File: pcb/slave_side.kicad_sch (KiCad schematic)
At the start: 71 parts, among them IC2 PCA9956BTWY, J4 4P4C_Shielded, SW20 SW_Push_45deg, SW21 SW_Push_45deg, SW22 SW_Push_45deg, SW23 SW_Push_45deg, SW24 SW_Push_45deg, SW25 SW_Push_45deg, SW26 SW_Push_45deg, SW27 SW_Push_45deg, SW28 SW_Push_45deg, SW29 SW_Push_45deg, SW30 SW_Push_45deg, SW31 SW_Push_45deg, SW32 SW_Push_45deg, SW33 SW_Push_45deg, SW34 SW_Push_45deg, SW35 SW_Push_45deg, SW36 SW_Push_45deg, SW37 SW_Push_45deg, U5 MCP23017T-E/ML, U6 NCP1117LPST33T3G, U7 OPT3001DNPR

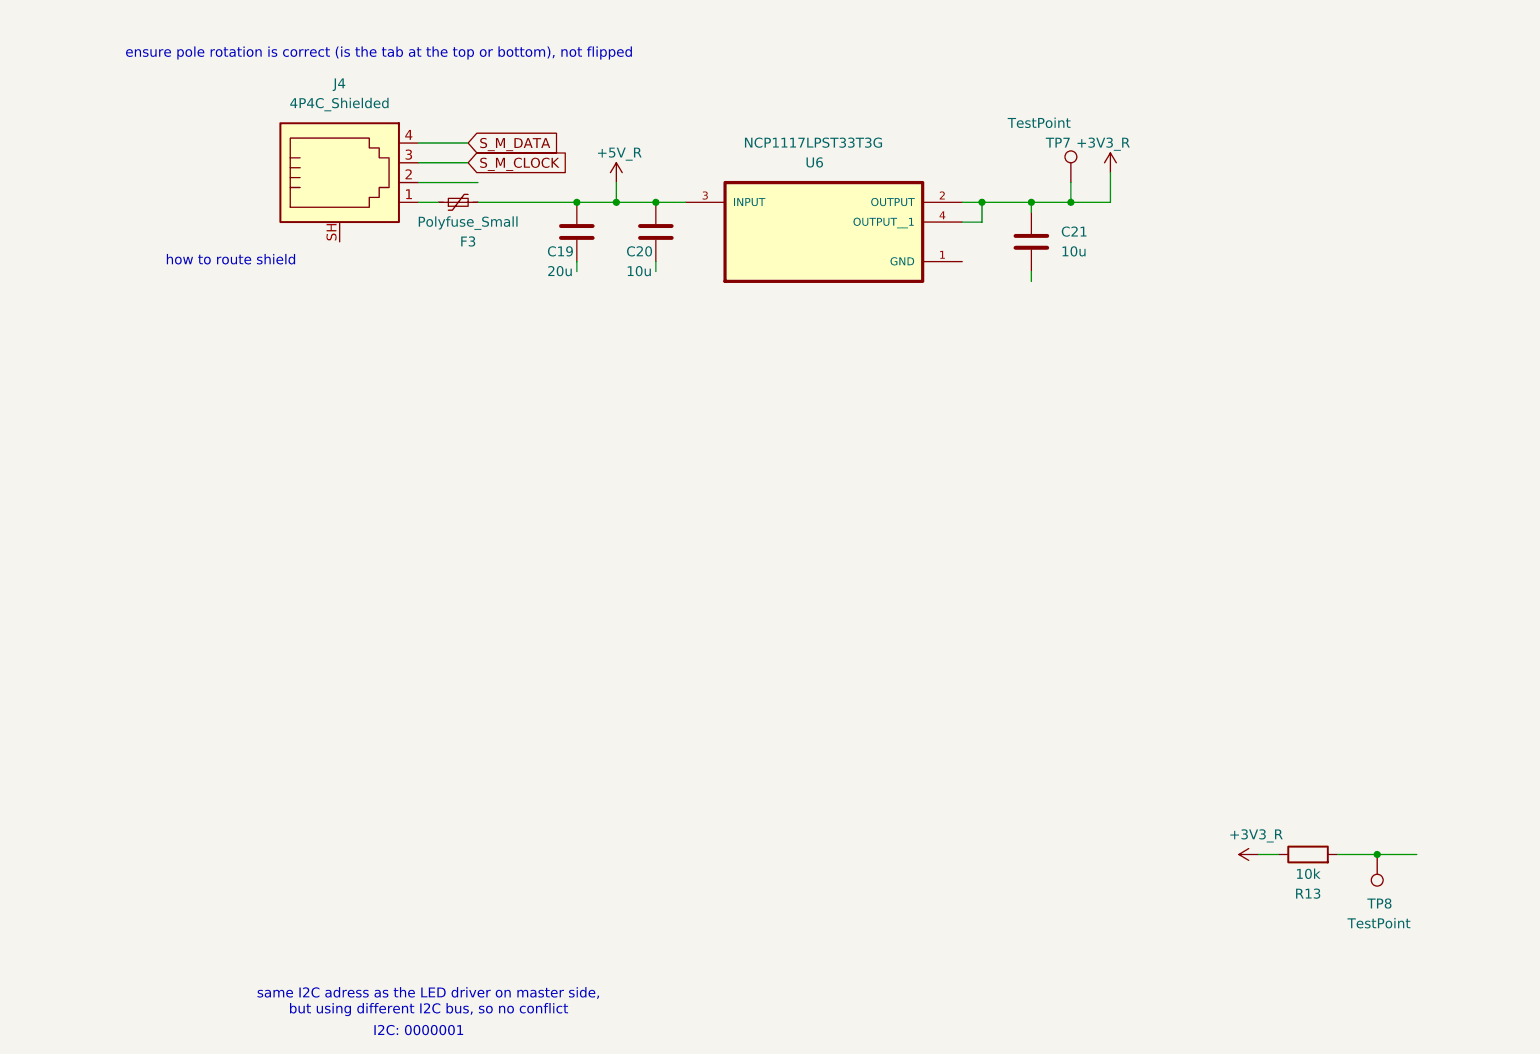
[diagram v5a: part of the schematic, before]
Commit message: fix: Proper MX LED footprint
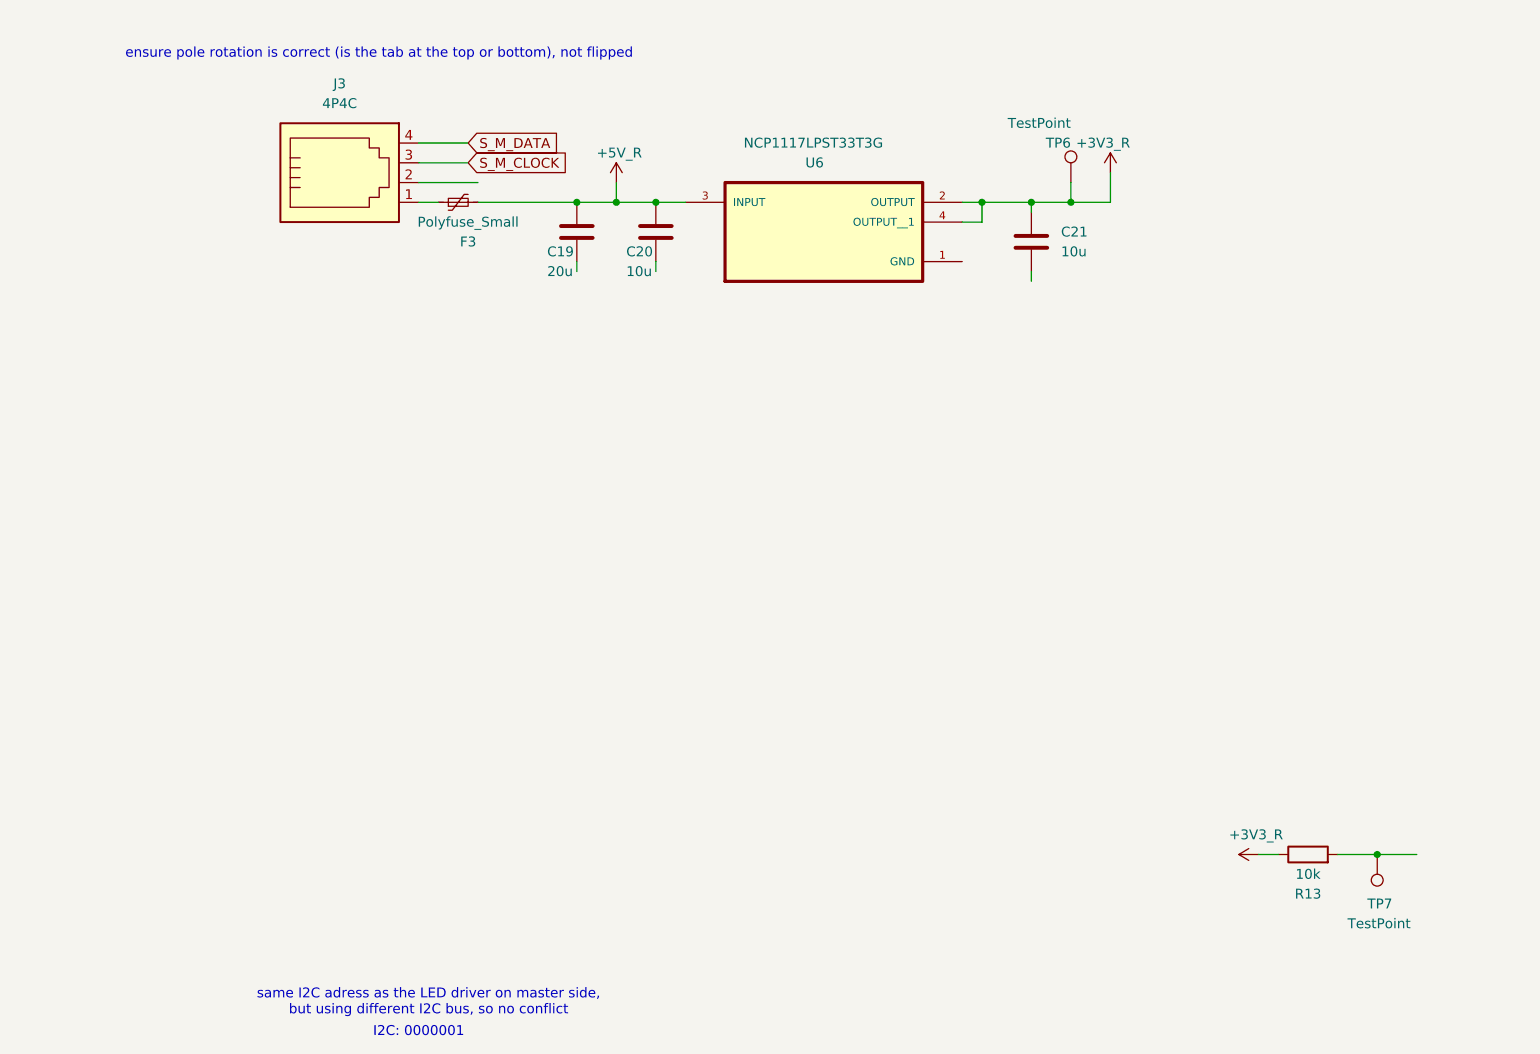
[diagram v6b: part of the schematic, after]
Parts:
- removed J4: 4P4C_Shielded, Connector_RJ:RJ9_Evercom_5301-440xxx_Horizontal, symbol Connector:4P4C_Shielded
- added J3: 4P4C, Connector_RJ:RJ9_Evercom_5301-440xxx_Horizontal, symbol Connector:4P4C
- SW20, SW21, SW22, SW23, SW24, SW25, SW26, SW27, SW28, SW29, SW30, SW31, SW32, SW33, SW34, SW35, SW36, SW37: footprint ai03-MX_V2:MX-Solderable-1U -> ai03-MX_V2:MX-LED
- renumbered TP7 to TP6, TP8 to TP7
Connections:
- net S_M_CLOCK: now also J3.3
- net S_M_DATA: now also J3.4
- net at F3.1: now also J3.1
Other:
- note removed: "how to route shield"
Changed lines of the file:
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@@
 		)
 	)
-	(text "how to route shield"
-		(exclude_from_sim no)
-		(at 36.83 44.45 0)
-		(effects
-			(font
-				(size 1.27 1.27)
-			)
-		)
-	)
 	(text "thermal pad under IC"
 		(exclude_from_sim no)
@@
 		(length 2.54)
 		(shape round)
-		(at 50.8 41.91 180)
-		(fields_autoplaced yes)
-		(effects
-			(font
-				(size 1.27 1.27)
-			)
-			(justify right bottom)
-		)
-		(property "Netclass" "R_GND"
-			(at 51.4985 44.45 0)
-			(effects
-				(font
-					(size 1.27 1.27)
-				)
-				(justify left)
-			)
-		)
-		(property "Component Class" ""
-			(at -242.57 -53.34 0)
-			(effects
-				(font
-					(size 1.27 1.27)
-					(italic yes)
-				)
-			)
-		)
-	)
-	(netclass_flag ""
-		(length 2.54)
-		(shape round)
 		(at 81.28 45.72 180)
 		(fields_autoplaced yes)
@@
 			)
 		)
-		(property "Footprint" "ai03-MX_V2:MX-Solderable-1U"
+		(property "Footprint" "ai03-MX_V2:MX-LED"
 			(at 375.92 67.31 0)
 			(effects
@@
 	)
 	(symbol
-		(lib_id "Connector:4P4C_Shielded")
-		(at 50.8 34.29 0)
-		(unit 1)
-		(exclude_from_sim no)
-		(in_bom yes)
-		(on_board yes)
-		(dnp no)
-		(fields_autoplaced yes)
-		(property "Reference" "J4"
-			(at 50.8 21.59 0)
-			(effects
-				(font
-					(size 1.27 1.27)
-				)
-			)
-		)
-		(property "Value" "4P4C_Shielded"
-			(at 50.8 24.13 0)
-			(effects
-				(font
-					(size 1.27 1.27)
-				)
-			)
-		)
-		(property "Footprint" "Connector_RJ:RJ9_Evercom_5301-440xxx_Horizontal"
-			(at 50.8 33.02 90)
-			(effects
-				(font
-					(size 1.27 1.27)
-				)
-				(hide yes)
-			)
-		)
-		(property "Datasheet" "~"
-			(at 50.8 33.02 90)
-			(effects
-				(font
-					(size 1.27 1.27)
-				)
-				(hide yes)
-			)
-		)
-		(property "Description" "RJ connector, 4P4C (4 positions 4 connected), RJ9/RJ10/RJ22, Shielded"
-			(at 50.8 34.29 0)
-			(effects
-				(font
-					(size 1.27 1.27)
-				)
-				(hide yes)
-			)
-		)
-		(pin "SH"
-		)
-		(pin "4"
-		)
-		(pin "3"
-		)
-		(pin "2"
-		)
-		(pin "1"
-		)
-		(instances
-			(project ""
-				(path "/2ec7cb33-7d00-426e-b710-cc42b1f2f810/84141690-5233-4517-90f0-209001a553bd"
-					(reference "J4")
-					(unit 1)
-				)
-			)
-		)
-	)
-	(symbol
 		(lib_id "Switch:SW_Push_45deg")
 		(at 364.49 39.37 0)
@@
 			)
 		)
-		(property "Footprint" "ai03-MX_V2:MX-Solderable-1U"
+		(property "Footprint" "ai03-MX_V2:MX-LED"
 			(at 364.49 39.37 0)
 			(effects
@@
 	)
 	(symbol
+		(lib_id "Connector:4P4C")
+		(at 50.8 34.29 0)
+		(unit 1)
+		(exclude_from_sim no)
+		(in_bom yes)
+		(on_board yes)
+		(dnp no)
+		(fields_autoplaced yes)
+		(property "Reference" "J3"
+			(at 50.8 21.59 0)
+			(effects
+				(font
+					(size 1.27 1.27)
+				)
+			)
+		)
+		(property "Value" "4P4C"
+			(at 50.8 24.13 0)
+			(effects
+				(font
+					(size 1.27 1.27)
+				)
+			)
+		)
+		(property "Footprint" "Connector_RJ:RJ9_Evercom_5301-440xxx_Horizontal"
+			(at 50.8 33.02 90)
+			(effects
+				(font
+					(size 1.27 1.27)
+				)
+				(hide yes)
+			)
+		)
+		(property "Datasheet" "~"
+			(at 50.8 33.02 90)
+			(effects
+				(font
+					(size 1.27 1.27)
+				)
+				(hide yes)
+			)
+		)
+		(property "Description" "RJ connector, 4P4C (4 positions 4 connected), RJ9/RJ10/RJ22"
+			(at 50.8 34.29 0)
+			(effects
+				(font
+					(size 1.27 1.27)
+				)
+				(hide yes)
+			)
+		)
+		(pin "3"
+		)
+		(pin "2"
+		)
+		(pin "1"
+		)
+		(pin "4"
+		)
+		(instances
+			(project "mSCKee"
+				(path "/2ec7cb33-7d00-426e-b710-cc42b1f2f810/84141690-5233-4517-90f0-209001a553bd"
+					(reference "J3")
+					(unit 1)
+				)
+			)
+		)
+	)
+	(symbol
 		(lib_id "Device:D_Small")
 		(at 401.32 44.45 270)
@@
 			)
 		)
-		(property "Footprint" "ai03-MX_V2:MX-Solderable-1U"
+		(property "Footprint" "ai03-MX_V2:MX-LED"
 			(at 341.63 39.37 0)
 			(effects
@@
 			)
 		)
-		(property "Footprint" "ai03-MX_V2:MX-Solderable-1U"
+		(property "Footprint" "ai03-MX_V2:MX-LED"
 			(at 353.06 39.37 0)
 			(effects
@@
 		(on_board yes)
 		(dnp no)
-		(property "Reference" "TP7"
+		(property "Reference" "TP6"
 			(at 144.78 29.21 0)
 			(effects
@@
 			(project "mSCKee"
 				(path "/2ec7cb33-7d00-426e-b710-cc42b1f2f810/84141690-5233-4517-90f0-209001a553bd"
-					(reference "TP7")
+					(reference "TP6")
 					(unit 1)
 				)
@@
 			)
 		)
-		(property "Footprint" "ai03-MX_V2:MX-Solderable-1U"
+		(property "Footprint" "ai03-MX_V2:MX-LED"
 			(at 387.35 67.31 0)
 			(effects
@@
 		(on_board yes)
 		(dnp no)
-		(property "Reference" "TP8"
+		(property "Reference" "TP7"
 			(at 182.88 127 0)
 			(effects
@@
 			(project ""
 				(path "/2ec7cb33-7d00-426e-b710-cc42b1f2f810/84141690-5233-4517-90f0-209001a553bd"
-					(reference "TP8")
+					(reference "TP7")
 					(unit 1)
 				)
@@
 			)
 		)
-		(property "Footprint" "ai03-MX_V2:MX-Solderable-1U"
+		(property "Footprint" "ai03-MX_V2:MX-LED"
 			(at 375.92 39.37 0)
 			(effects
@@
 			)
 		)
-		(property "Footprint" "ai03-MX_V2:MX-Solderable-1U"
+		(property "Footprint" "ai03-MX_V2:MX-LED"
 			(at 387.35 53.34 0)
 			(effects
@@
 			)
 		)
-		(property "Footprint" "ai03-MX_V2:MX-Solderable-1U"
+		(property "Footprint" "ai03-MX_V2:MX-LED"
 			(at 364.49 67.31 0)
 			(effects
@@
 			)
 		)
-		(property "Footprint" "ai03-MX_V2:MX-Solderable-1U"
+		(property "Footprint" "ai03-MX_V2:MX-LED"
 			(at 364.49 53.34 0)
 			(effects
@@
 			)
 		)
-		(property "Footprint" "ai03-MX_V2:MX-Solderable-1U"
+		(property "Footprint" "ai03-MX_V2:MX-LED"
 			(at 341.63 67.31 0)
 			(effects
@@
 			)
 		)
-		(property "Footprint" "ai03-MX_V2:MX-Solderable-1U"
+		(property "Footprint" "ai03-MX_V2:MX-LED"
 			(at 353.06 53.34 0)
 			(effects
@@
 			)
 		)
-		(property "Footprint" "ai03-MX_V2:MX-Solderable-1U"
+		(property "Footprint" "ai03-MX_V2:MX-LED"
 			(at 375.92 53.34 0)
 			(effects
@@
 			)
 		)
-		(property "Footprint" "ai03-MX_V2:MX-Solderable-1U"
+		(property "Footprint" "ai03-MX_V2:MX-LED"
 			(at 353.06 67.31 0)
 			(effects
@@
 			)
 		)
-		(property "Footprint" "ai03-MX_V2:MX-Solderable-1U"
+		(property "Footprint" "ai03-MX_V2:MX-LED"
 			(at 387.35 39.37 0)
 			(effects
@@
 			)
 		)
-		(property "Footprint" "ai03-MX_V2:MX-Solderable-1U"
+		(property "Footprint" "ai03-MX_V2:MX-LED"
 			(at 398.78 39.37 0)
 			(effects
@@
 			)
 		)
-		(property "Footprint" "ai03-MX_V2:MX-Solderable-1U"
+		(property "Footprint" "ai03-MX_V2:MX-LED"
 			(at 398.78 53.34 0)
 			(effects
@@
 			)
 		)
-		(property "Footprint" "ai03-MX_V2:MX-Solderable-1U"
+		(property "Footprint" "ai03-MX_V2:MX-LED"
 			(at 341.63 53.34 0)
 			(effects
@@
 			)
 		)
-		(property "Footprint" "ai03-MX_V2:MX-Solderable-1U"
+		(property "Footprint" "ai03-MX_V2:MX-LED"
 			(at 398.78 67.31 0)
 			(effects

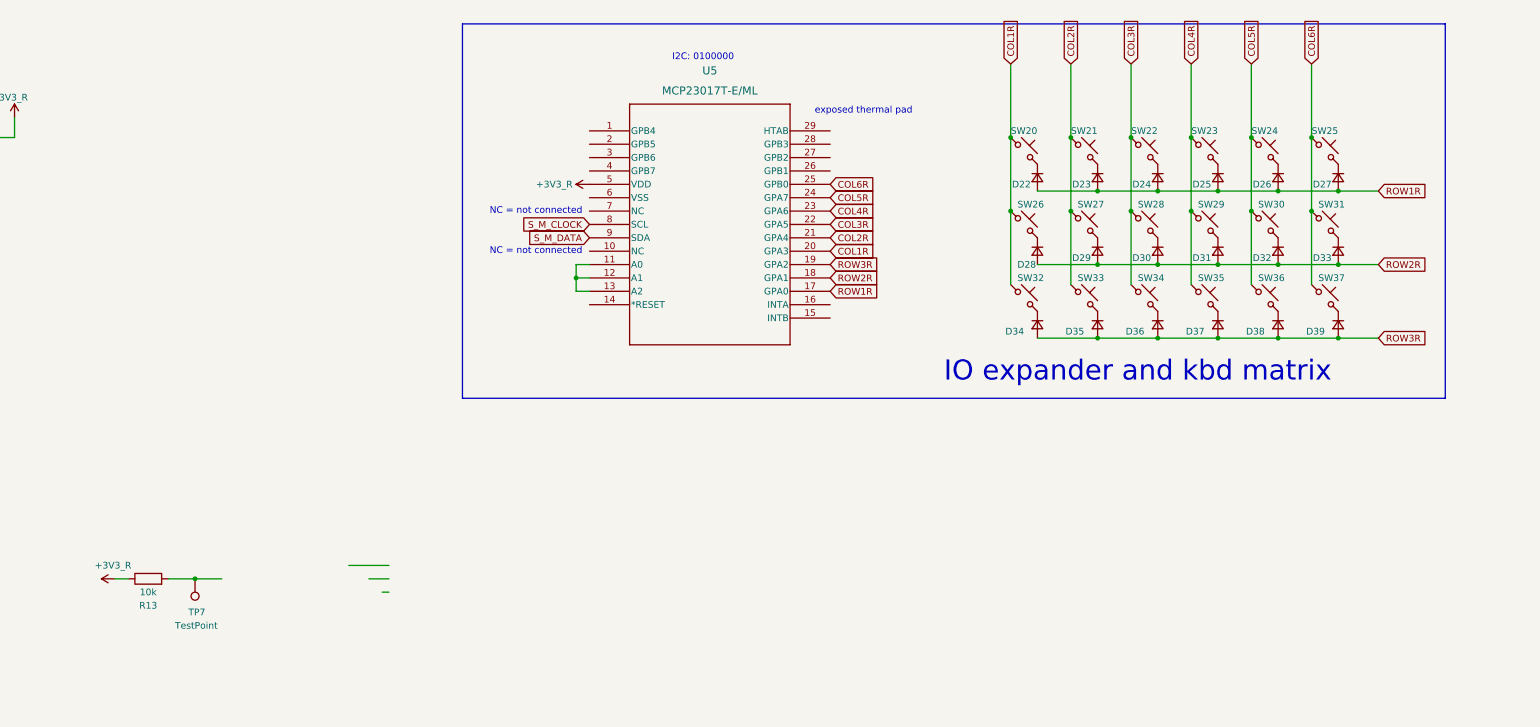
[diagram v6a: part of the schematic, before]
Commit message: fix: revert to proper switch footprint without SMD LED
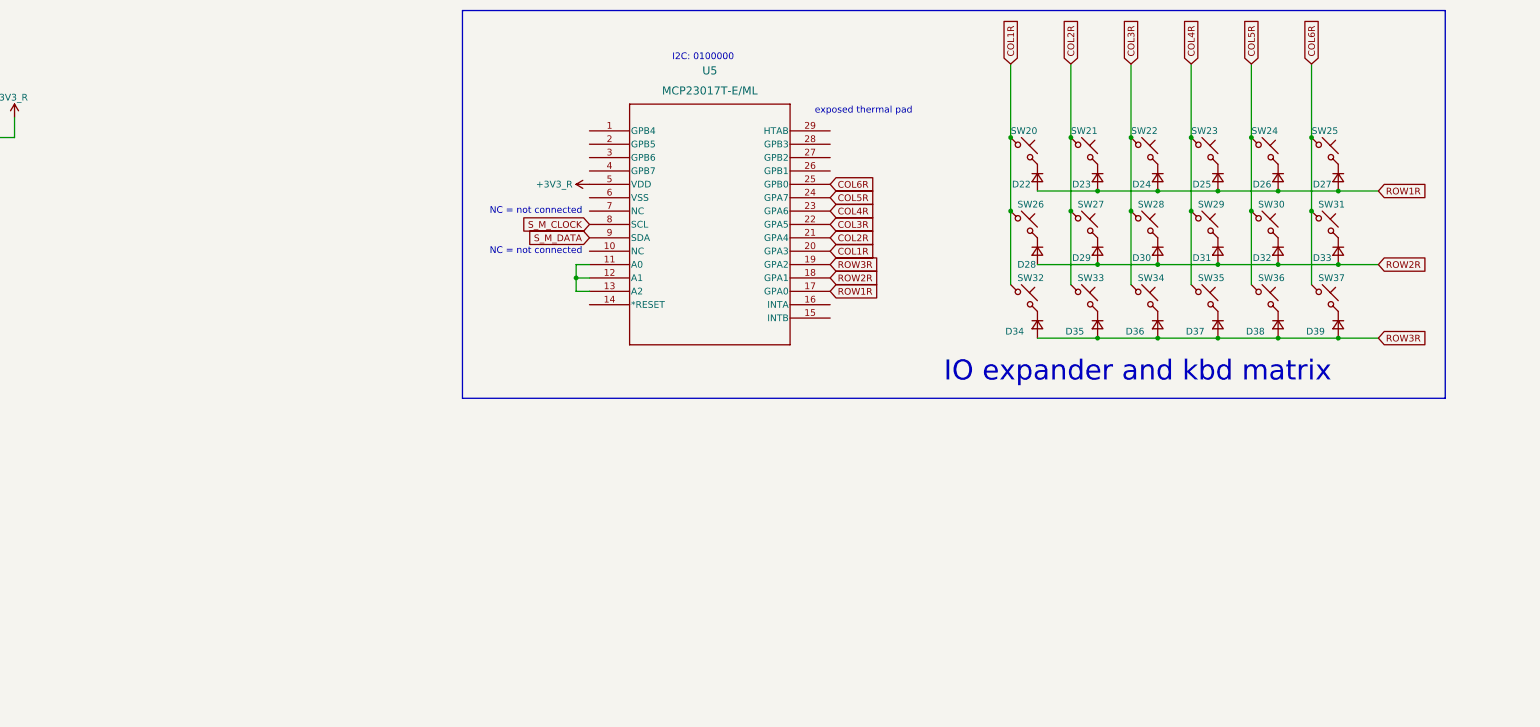
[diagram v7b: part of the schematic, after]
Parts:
- removed R13: 10k, Resistor_SMD:R_0402_1005Metric, symbol library:R
- removed TP7: TestPoint, TestPoint:TestPoint_Pad_D2.0mm, symbol Connector:TestPoint
- SW20, SW21, SW22, SW23, SW24, SW25, SW26, SW27, SW28, SW29, SW30, SW31, SW32, SW33, SW34, SW35, SW36, SW37: footprint ai03-MX_V2:MX-LED -> ai03-MX_V2:MX-Solderable-1U

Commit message: fix: OE pin PCA9956B control on startup
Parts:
- added R15: 2k, Resistor_SMD:R_0402_1005Metric, symbol library:R
- added R17: 10k, Resistor_SMD:R_0402_1005Metric, symbol library:R
- D38: renamed from D22; footprint (none) -> Diode_SMD:D_0201_0603Metric
- D39: renamed from D23; footprint (none) -> Diode_SMD:D_0201_0603Metric
- D40: renamed from D24; footprint (none) -> Diode_SMD:D_0201_0603Metric
- D41: renamed from D25; footprint (none) -> Diode_SMD:D_0201_0603Metric
- D42: renamed from D26; footprint (none) -> Diode_SMD:D_0201_0603Metric
- D43: renamed from D27; footprint (none) -> Diode_SMD:D_0201_0603Metric
- D44: renamed from D28; footprint (none) -> Diode_SMD:D_0201_0603Metric
- D45: renamed from D29; footprint (none) -> Diode_SMD:D_0201_0603Metric
- D46: renamed from D30; footprint (none) -> Diode_SMD:D_0201_0603Metric
- D47: renamed from D31; footprint (none) -> Diode_SMD:D_0201_0603Metric
- D48: renamed from D32; footprint (none) -> Diode_SMD:D_0201_0603Metric
- D49: renamed from D33; footprint (none) -> Diode_SMD:D_0201_0603Metric
- D50: renamed from D34; footprint (none) -> Diode_SMD:D_0201_0603Metric
- D51: renamed from D35; footprint (none) -> Diode_SMD:D_0201_0603Metric
- D52: renamed from D36; footprint (none) -> Diode_SMD:D_0201_0603Metric
- D53: renamed from D37; footprint (none) -> Diode_SMD:D_0201_0603Metric
- D54: renamed from D38; footprint (none) -> Diode_SMD:D_0201_0603Metric
- D55: renamed from D39; footprint (none) -> Diode_SMD:D_0201_0603Metric
- D56: renamed from D40; footprint (none) -> LED_SMD:LED_0603_1608Metric
- D57: renamed from D41; footprint (none) -> LED_SMD:LED_0603_1608Metric
- D58: renamed from D42; footprint (none) -> LED_SMD:LED_0603_1608Metric
- D59: renamed from D43; footprint (none) -> LED_SMD:LED_0603_1608Metric
- D60: renamed from D44; footprint (none) -> LED_SMD:LED_0603_1608Metric
- D61: renamed from D45; footprint (none) -> LED_SMD:LED_0603_1608Metric
- D62: renamed from D46; footprint (none) -> LED_SMD:LED_0603_1608Metric
- D63: renamed from D47; footprint (none) -> LED_SMD:LED_0603_1608Metric
- D64: renamed from D48; footprint (none) -> LED_SMD:LED_0603_1608Metric
- D65: renamed from D49; footprint (none) -> LED_SMD:LED_0603_1608Metric
- D66: renamed from D50; footprint (none) -> LED_SMD:LED_0603_1608Metric
- D67: renamed from D51; footprint (none) -> LED_SMD:LED_0603_1608Metric
- D68: renamed from D52; footprint (none) -> LED_SMD:LED_0603_1608Metric
- D69: renamed from D53; footprint (none) -> LED_SMD:LED_0603_1608Metric
- D70: renamed from D54; footprint (none) -> LED_SMD:LED_0603_1608Metric
- D71: renamed from D55; footprint (none) -> LED_SMD:LED_0603_1608Metric
- D72: renamed from D56; footprint (none) -> LED_SMD:LED_0603_1608Metric
- D73: renamed from D57; footprint (none) -> LED_SMD:LED_0603_1608Metric
- D74: renamed from D58; footprint (none) -> LED_SMD:LED_0603_1608Metric
- D75: renamed from D59; footprint (none) -> LED_SMD:LED_0603_1608Metric
- D76: renamed from D60; footprint (none) -> LED_SMD:LED_0603_1608Metric
- renumbered J3 to J4, R14 to R16
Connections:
- net +3V3_R: now also R16.2, R15.1, R17.1
- net OE_ENABLE_R: now reaches R16.1
- net OE_ENABLE_R: now also IC2.5 (OE), U5.26 (GPB1)
- net at IC2.1 (REXT): now also R15.2
- net at IC2.35 (RESET): now also R17.2
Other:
- moved on the sheet: IC2, R16
